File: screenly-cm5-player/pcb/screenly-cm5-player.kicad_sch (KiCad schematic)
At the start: 0 parts

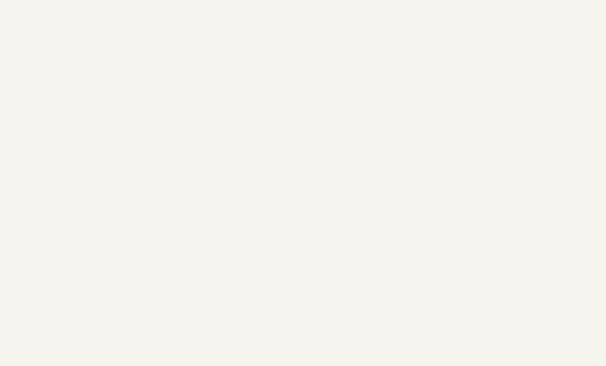
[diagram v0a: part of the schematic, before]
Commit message: Power stage completed
All power stage has been completed. It has 3 different controlled
outputs USB and PCIe power are separated from the main power due to
safety, durability and cost reasons. PCIe will be DNP later.
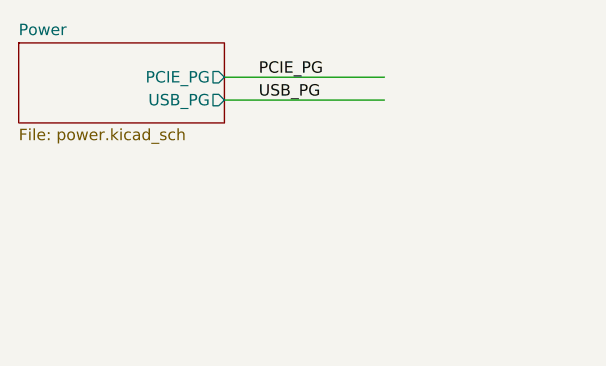
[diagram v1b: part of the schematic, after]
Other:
- added sheet Power (power.kicad_sch)
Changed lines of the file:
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@@
 		(company "Screenly Inc.")
+	)
+	(wire
+		(pts
+			(xy 48.26 39.37) (xy 66.04 39.37)
+		)
+		(stroke
+			(width 0)
+			(type default)
+		)
+	)
+	(wire
+		(pts
+			(xy 48.26 36.83) (xy 66.04 36.83)
+		)
+		(stroke
+			(width 0)
+			(type default)
+		)
+	)
+	(label "USB_PG"
+		(at 52.07 39.37 0)
+		(effects
+			(font
+				(size 1.27 1.27)
+			)
+			(justify left bottom)
+		)
+	)
+	(label "PCIE_PG"
+		(at 52.07 36.83 0)
+		(effects
+			(font
+				(size 1.27 1.27)
+			)
+			(justify left bottom)
+		)
 	)
 	(sheet
@@
 				)
 			)
+		)
+	)
+	(sheet
+		(at 25.4 33.02)
+		(size 22.86 8.89)
+		(exclude_from_sim no)
+		(in_bom yes)
+		(on_board yes)
+		(dnp no)
+		(fields_autoplaced yes)
+		(stroke
+			(width 0.1524)
+			(type solid)
+		)
+		(fill
+			(color 0 0 0 0)
+		)
+		(property "Sheetname" "Power"
+			(at 25.4 32.3084 0)
+			(show_name no)
+			(do_not_autoplace no)
+			(effects
+				(font
+					(size 1.27 1.27)
+				)
+				(justify left bottom)
+			)
+		)
+		(property "Sheetfile" "power.kicad_sch"
+			(at 25.4 42.4946 0)
+			(show_name no)
+			(do_not_autoplace no)
+			(effects
+				(font
+					(size 1.27 1.27)
+				)
+				(justify left top)
+			)
+		)
+		(pin "PCIE_PG" output
+			(at 48.26 36.83 0)
+			(effects
+				(font
+					(size 1.27 1.27)
+				)
+				(justify right)
+			)
+		)
+		(pin "USB_PG" output
+			(at 48.26 39.37 0)
+			(effects
+				(font
+					(size 1.27 1.27)
+				)
+				(justify right)
+			)
+		)
+		(instances
+			(project "screenly-cm5-player"
+				(path "/e8a2875a-18ea-4799-b56d-ecb6ae09ef8e"
+					(page "3")
+				)
+			)

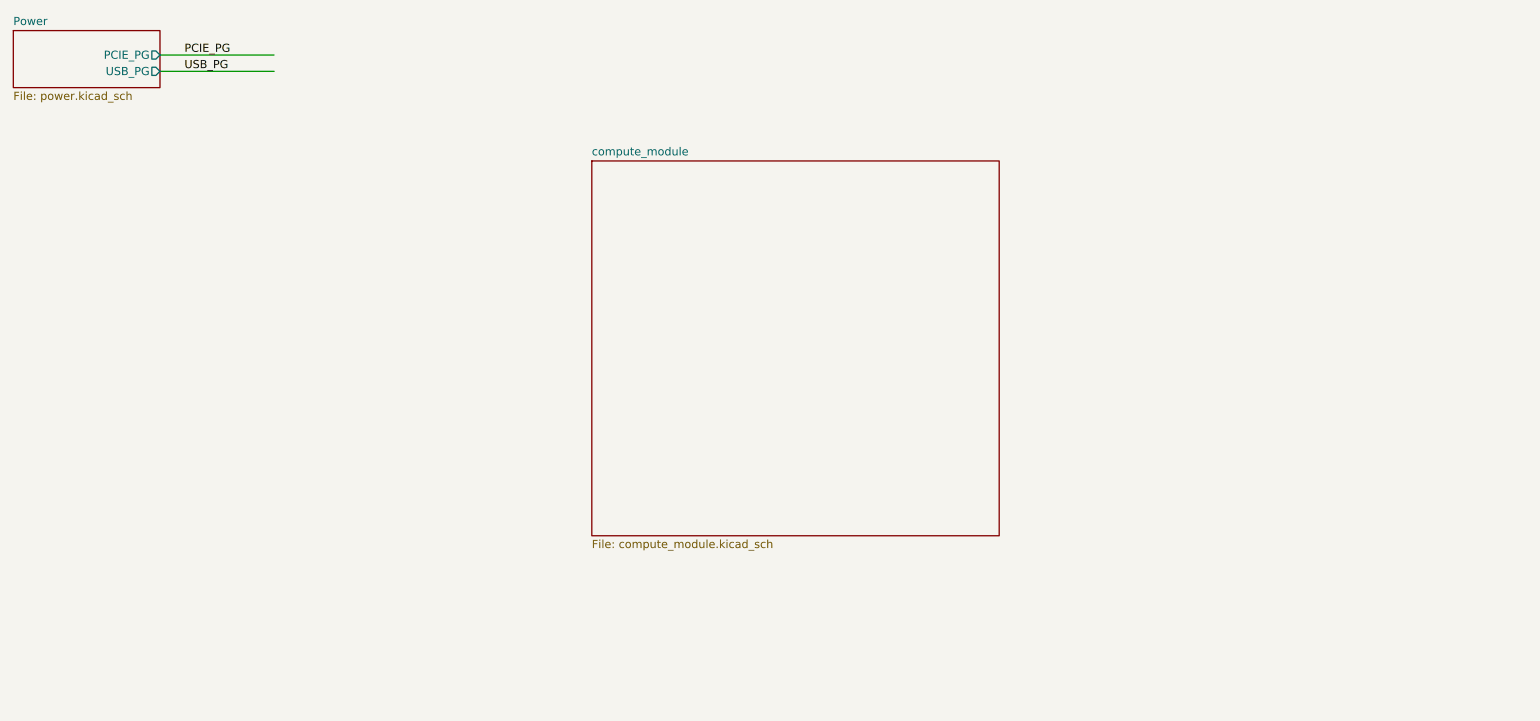
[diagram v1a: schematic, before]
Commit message: Ethernet and PCIe sections are done.
Modified power section and moved PCIe specific circuit into its own
section.
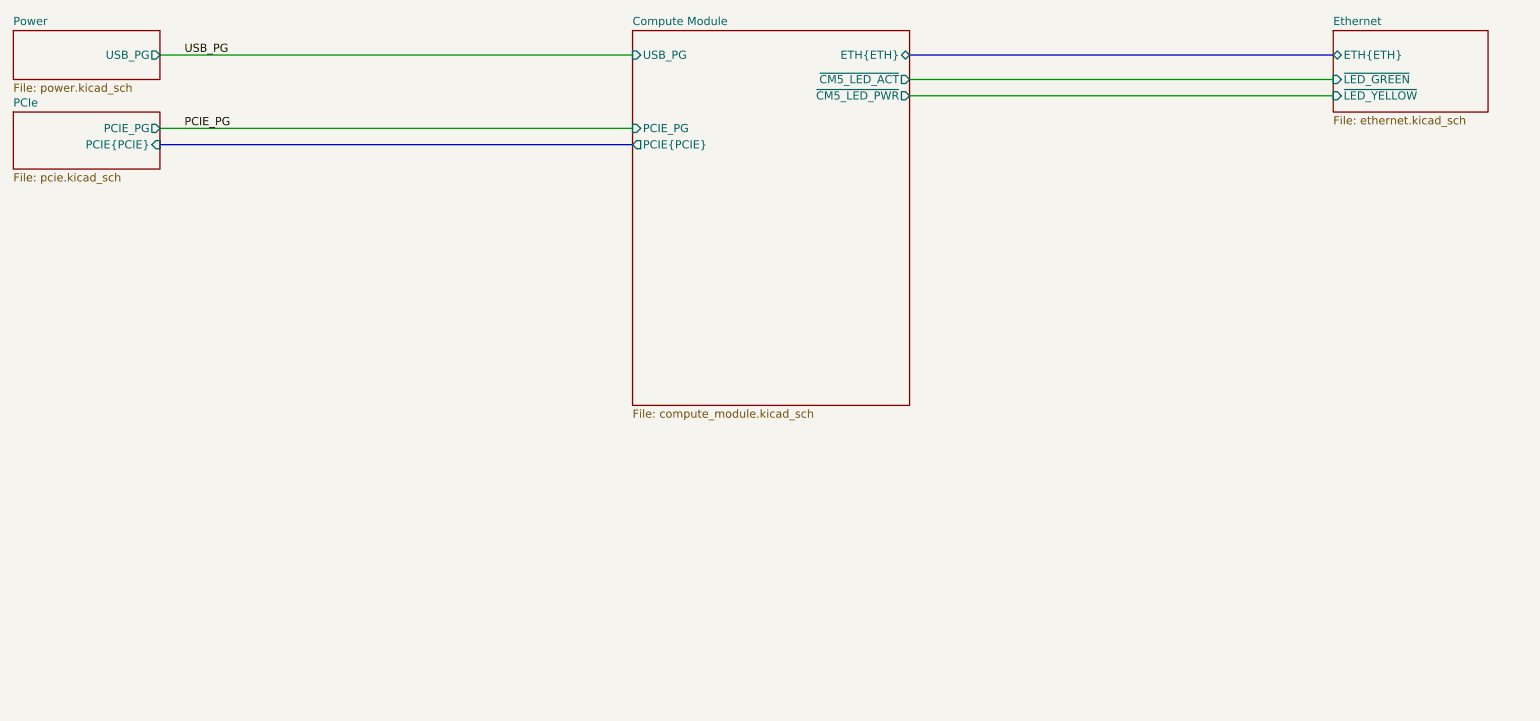
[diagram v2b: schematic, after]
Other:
- sheet compute_module renamed Compute Module
- added sheet Ethernet (ethernet.kicad_sch)
- added sheet PCIe (pcie.kicad_sch)
- sheet Compute Module ports: added ETH{ETH}, PCIE_PG, PCIE{PCIE}, USB_PG, ~{CM5_LED_ACT}, ~{CM5_LED_PWR}; removed none
- sheet Power ports: added none; removed PCIE_PG
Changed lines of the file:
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@@
 	(wire
 		(pts
-			(xy 48.26 39.37) (xy 66.04 39.37)
+			(xy 165.1 43.18) (xy 231.14 43.18)
 		)
 		(stroke
@@
 	(wire
 		(pts
-			(xy 48.26 36.83) (xy 66.04 36.83)
+			(xy 165.1 40.64) (xy 231.14 40.64)
+		)
+		(stroke
+			(width 0)
+			(type default)
+		)
+	)
+	(bus
+		(pts
+			(xy 165.1 36.83) (xy 231.14 36.83)
+		)
+		(stroke
+			(width 0)
+			(type default)
+		)
+	)
+	(wire
+		(pts
+			(xy 48.26 36.83) (xy 121.92 36.83)
+		)
+		(stroke
+			(width 0)
+			(type default)
+		)
+	)
+	(wire
+		(pts
+			(xy 48.26 48.26) (xy 121.92 48.26)
+		)
+		(stroke
+			(width 0)
+			(type default)
+		)
+	)
+	(bus
+		(pts
+			(xy 48.26 50.8) (xy 121.92 50.8)
 		)
 		(stroke
@@
 	)
 	(label "USB_PG"
-		(at 52.07 39.37 0)
-		(effects
-			(font
-				(size 1.27 1.27)
-			)
-			(justify left bottom)
-		)
-	)
-	(label "PCIE_PG"
 		(at 52.07 36.83 0)
 		(effects
@@
 		)
 	)
+	(label "PCIE_PG"
+		(at 52.07 48.26 0)
+		(effects
+			(font
+				(size 1.27 1.27)
+			)
+			(justify left bottom)
+		)
+	)
 	(sheet
-		(at 115.57 53.34)
-		(size 63.5 58.42)
-		(exclude_from_sim no)
-		(in_bom yes)
-		(on_board yes)
-		(dnp no)
-		(fields_autoplaced yes)
-		(stroke
-			(width 0.1524)
-			(type solid)
-		)
-		(fill
-			(color 0 0 0 0)
-		)
-		(property "Sheetname" "compute_module"
-			(at 115.57 52.6284 0)
-			(show_name no)
-			(do_not_autoplace no)
-			(effects
-				(font
-					(size 1.27 1.27)
-				)
-				(justify left bottom)
-			)
-		)
-		(property "Sheetfile" "compute_module.kicad_sch"
-			(at 115.57 112.3446 0)
-			(show_name no)
-			(do_not_autoplace no)
-			(effects
-				(font
-					(size 1.27 1.27)
-				)
-				(justify left top)
-			)
-		)
-		(instances
-			(project "screenly-cm5-player"
-				(path "/e8a2875a-18ea-4799-b56d-ecb6ae09ef8e"
-					(page "2")
-				)
-			)
-		)
-	)
-	(sheet
-		(at 25.4 33.02)
+		(at 25.4 45.72)
 		(size 22.86 8.89)
 		(exclude_from_sim no)
@@
 			(color 0 0 0 0)
 		)
+		(property "Sheetname" "PCIe"
+			(at 25.4 45.0084 0)
+			(show_name no)
+			(do_not_autoplace no)
+			(effects
+				(font
+					(size 1.27 1.27)
+				)
+				(justify left bottom)
+			)
+		)
+		(property "Sheetfile" "pcie.kicad_sch"
+			(at 25.4 55.1946 0)
+			(show_name no)
+			(do_not_autoplace no)
+			(effects
+				(font
+					(size 1.27 1.27)
+				)
+				(justify left top)
+			)
+		)
+		(pin "PCIE{PCIE}" input
+			(at 48.26 50.8 0)
+			(effects
+				(font
+					(size 1.27 1.27)
+				)
+				(justify right)
+			)
+		)
+		(pin "PCIE_PG" output
+			(at 48.26 48.26 0)
+			(effects
+				(font
+					(size 1.27 1.27)
+				)
+				(justify right)
+			)
+		)
+		(instances
+			(project "screenly-cm5-player"
+				(path "/e8a2875a-18ea-4799-b56d-ecb6ae09ef8e"
+					(page "5")
+				)
+			)
+		)
+	)
+	(sheet
+		(at 121.92 33.02)
+		(size 43.18 58.42)
+		(exclude_from_sim no)
+		(in_bom yes)
+		(on_board yes)
+		(dnp no)
+		(fields_autoplaced yes)
+		(stroke
+			(width 0.1524)
+			(type solid)
+		)
+		(fill
+			(color 0 0 0 0)
+		)
+		(property "Sheetname" "Compute Module"
+			(at 121.92 32.3084 0)
+			(show_name no)
+			(do_not_autoplace no)
+			(effects
+				(font
+					(size 1.27 1.27)
+				)
+				(justify left bottom)
+			)
+		)
+		(property "Sheetfile" "compute_module.kicad_sch"
+			(at 121.92 92.0246 0)
+			(show_name no)
+			(do_not_autoplace no)
+			(effects
+				(font
+					(size 1.27 1.27)
+				)
+				(justify left top)
+			)
+		)
+		(pin "~{CM5_LED_PWR}" output
+			(at 165.1 43.18 0)
+			(effects
+				(font
+					(size 1.27 1.27)
+				)
+				(justify right)
+			)
+		)
+		(pin "ETH{ETH}" bidirectional
+			(at 165.1 36.83 0)
+			(effects
+				(font
+					(size 1.27 1.27)
+				)
+				(justify right)
+			)
+		)
+		(pin "~{CM5_LED_ACT}" output
+			(at 165.1 40.64 0)
+			(effects
+				(font
+					(size 1.27 1.27)
+				)
+				(justify right)
+			)
+		)
+		(pin "PCIE_PG" input
+			(at 121.92 48.26 180)
+			(effects
+				(font
+					(size 1.27 1.27)
+				)
+				(justify left)
+			)
+		)
+		(pin "USB_PG" input
+			(at 121.92 36.83 180)
+			(effects
+				(font
+					(size 1.27 1.27)
+				)
+				(justify left)
+			)
+		)
+		(pin "PCIE{PCIE}" output
+			(at 121.92 50.8 180)
+			(effects
+				(font
+					(size 1.27 1.27)
+				)
+				(justify left)
+			)
+		)
+		(instances
+			(project "screenly-cm5-player"
+				(path "/e8a2875a-18ea-4799-b56d-ecb6ae09ef8e"
+					(page "2")
+				)
+			)
+		)
+	)
+	(sheet
+		(at 25.4 33.02)
+		(size 22.86 7.62)
+		(exclude_from_sim no)
+		(in_bom yes)
+		(on_board yes)
+		(dnp no)
+		(fields_autoplaced yes)
+		(stroke
+			(width 0.1524)
+			(type solid)
+		)
+		(fill
+			(color 0 0 0 0)
+		)
 		(property "Sheetname" "Power"
 			(at 25.4 32.3084 0)
@@
 		)
 		(property "Sheetfile" "power.kicad_sch"
-			(at 25.4 42.4946 0)
+			(at 25.4 41.2246 0)
 			(show_name no)
 			(do_not_autoplace no)
@@
 			)
 		)
-		(pin "PCIE_PG" output
+		(pin "USB_PG" output
 			(at 48.26 36.83 0)
-			(effects
-				(font
-					(size 1.27 1.27)
-				)
-				(justify right)
-			)
-		)
-		(pin "USB_PG" output
-			(at 48.26 39.37 0)
 			(effects
 				(font
@@
 				)
 			)
+		)
+	)
+	(sheet
+		(at 231.14 33.02)
+		(size 24.13 12.7)
+		(exclude_from_sim no)
+		(in_bom yes)
+		(on_board yes)
+		(dnp no)
+		(fields_autoplaced yes)
+		(stroke
+			(width 0.1524)
+			(type solid)
+		)
+		(fill
+			(color 0 0 0 0)
+		)
+		(property "Sheetname" "Ethernet"
+			(at 231.14 32.3084 0)
+			(show_name no)
+			(do_not_autoplace no)
+			(effects
+				(font
+					(size 1.27 1.27)
+				)
+				(justify left bottom)
+			)
+		)
+		(property "Sheetfile" "ethernet.kicad_sch"
+			(at 231.14 46.3046 0)
+			(show_name no)
+			(do_not_autoplace no)
+			(effects
+				(font
+					(size 1.27 1.27)
+				)
+				(justify left top)
+			)
+		)
+		(pin "ETH{ETH}" bidirectional
+			(at 231.14 36.83 180)
+			(effects
+				(font
+					(size 1.27 1.27)
+				)
+				(justify left)
+			)
+		)
+		(pin "~{LED_GREEN}" input
+			(at 231.14 40.64 180)
+			(effects
+				(font
+					(size 1.27 1.27)
+				)
+				(justify left)
+			)
+		)
+		(pin "~{LED_YELLOW}" input
+			(at 231.14 43.18 180)
+			(effects
+				(font
+					(size 1.27 1.27)
+				)
+				(justify left)
+			)
+		)
+		(instances
+			(project "screenly-cm5-player"
+				(path "/e8a2875a-18ea-4799-b56d-ecb6ae09ef8e"
+					(page "4")
+				)
+			)

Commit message: WIP Schematics
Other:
- added sheet HDMI (hdmi.kicad_sch)
- added sheet USB (usb.kicad_sch)
- sheet Compute Module ports: added HDMI0{HDMI}, HDMI1{HDMI}, USB2{USB}, USB3_0{USB3}, USB3_1{USB3}, ~{ETH_LED_ACT}, ~{ETH_LED_SPD}, ~{HDMI0_PWR_FAULT}, ~{HDMI1_PWR_FAULT}, ~{USB3_0_PWR_FAULT}, ~{USB3_1_PWR_FAULT}, ~{USBA_PWR_FAULT}; removed ~{CM5_LED_ACT}, ~{CM5_LED_PWR}

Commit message: Finished USB
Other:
- sheet USB renamed USB3_0
- added sheet USB2 (usb2.kicad_sch)
- added sheet USB3_1 (usb3_1.kicad_sch)
- sheet USB3_0: file usb.kicad_sch -> usb3_0.kicad_sch
- sheet USB3_0 ports: added none; removed USB2{USB}, USB3_1{USB3}, ~{USB3_1_PWR_FAULT}, ~{USBA_PWR_FAULT}

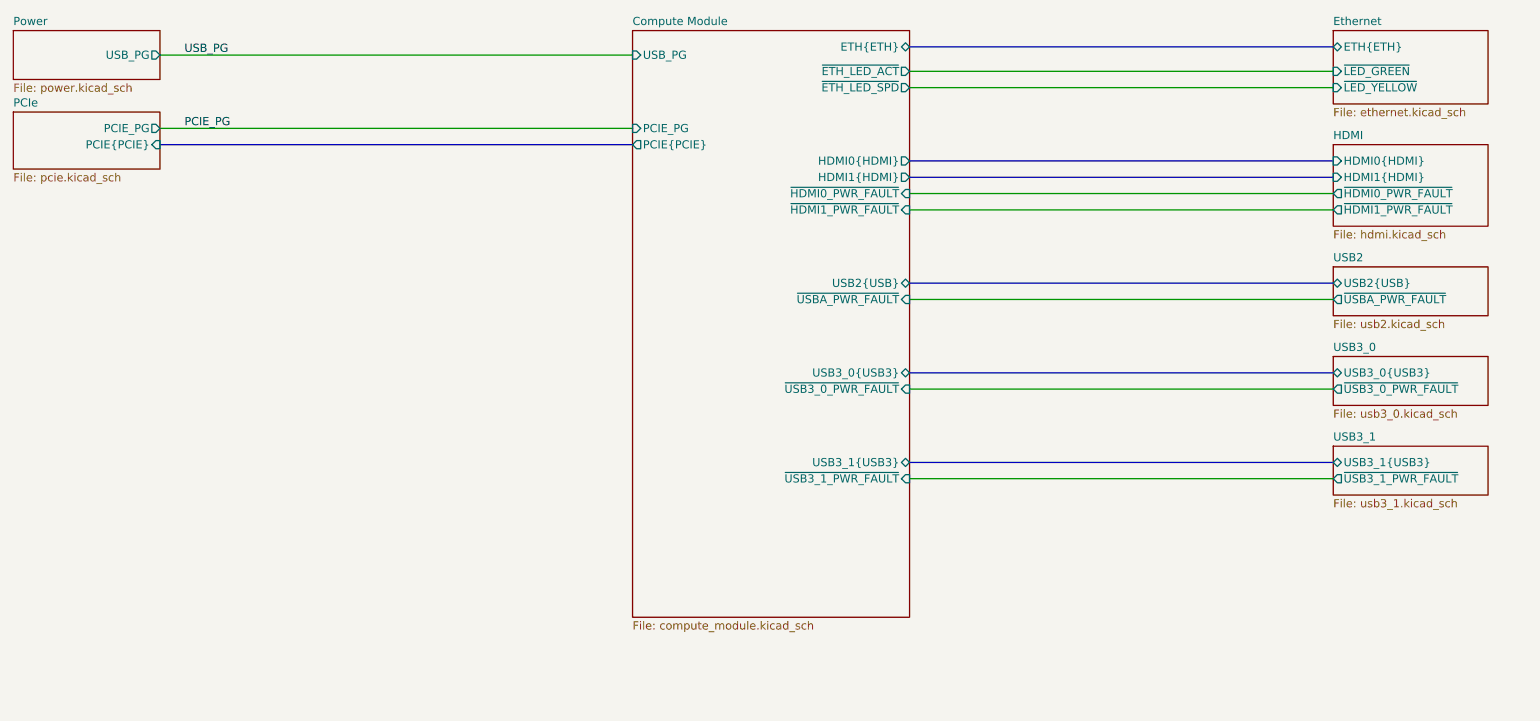
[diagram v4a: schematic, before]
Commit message: Revised USB design 1xUSB-C 2.0, 2xUSB-A 3.0
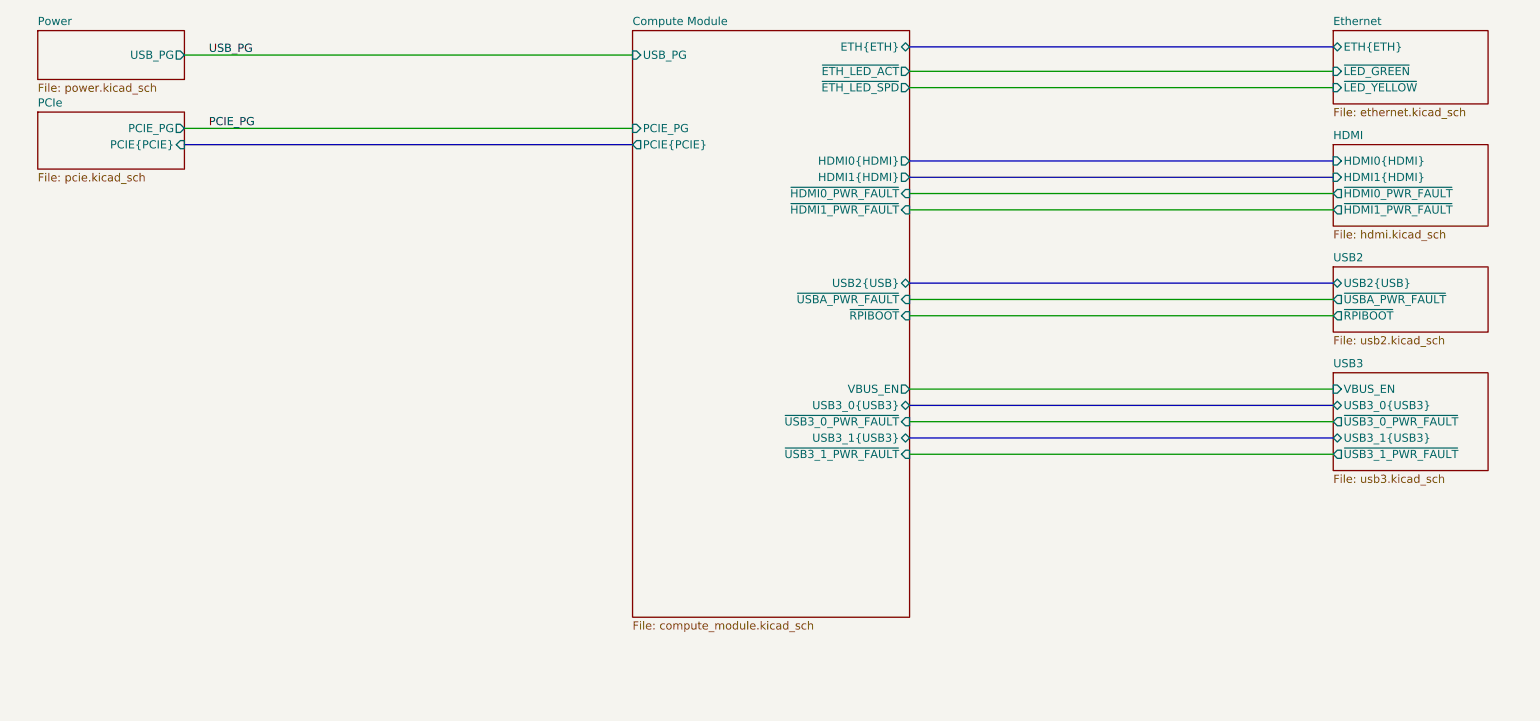
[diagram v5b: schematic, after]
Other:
- sheet USB3_0 renamed USB3
- removed sheet USB3_1
- sheet Compute Module ports: added VBUS_EN, ~{RPIBOOT}; removed none
- sheet USB2 ports: added ~{RPIBOOT}; removed none
- sheet USB3: file usb3_0.kicad_sch -> usb3.kicad_sch
- sheet USB3 ports: added USB3_1{USB3}, VBUS_EN, ~{USB3_1_PWR_FAULT}; removed none

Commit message: Finished schematics design.
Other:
- added sheet Analog Audio (analog_audio.kicad_sch)
- added sheet EEPROM (eeprom.kicad_sch)
- added sheet SDCard (sdcard.kicad_sch)
- added sheet TPM (tpm.kicad_sch)
- added sheet User Interface (user_interface.kicad_sch)
- sheet Compute Module ports: added Audio{I2S}, EE_SCL, EE_SDA, PWR_BTN, SD_CARD{SDIO}, TPM{SPI}, ~{CM5_LED_ACT}, ~{CM5_LED_PWR}, ~{FACTORY_RST_BTN}, ~{TPM_PIRQ}, ~{TPM_RST}, ~{USB2_PWR_FAULT}; removed ~{USBA_PWR_FAULT}
- sheet USB2 ports: added ~{USB2_PWR_FAULT}; removed ~{USBA_PWR_FAULT}
